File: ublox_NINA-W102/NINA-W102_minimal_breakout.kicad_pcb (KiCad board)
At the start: 2 copper layers, 47 x 20.7 mm, 17 parts, among them J1 Conn_01x15, J2 Conn_01x15, J3 6_PIN_SERIAL_TARGETLOCK, SW1 BOOT, SW2 RESET, U1 NINA-W102

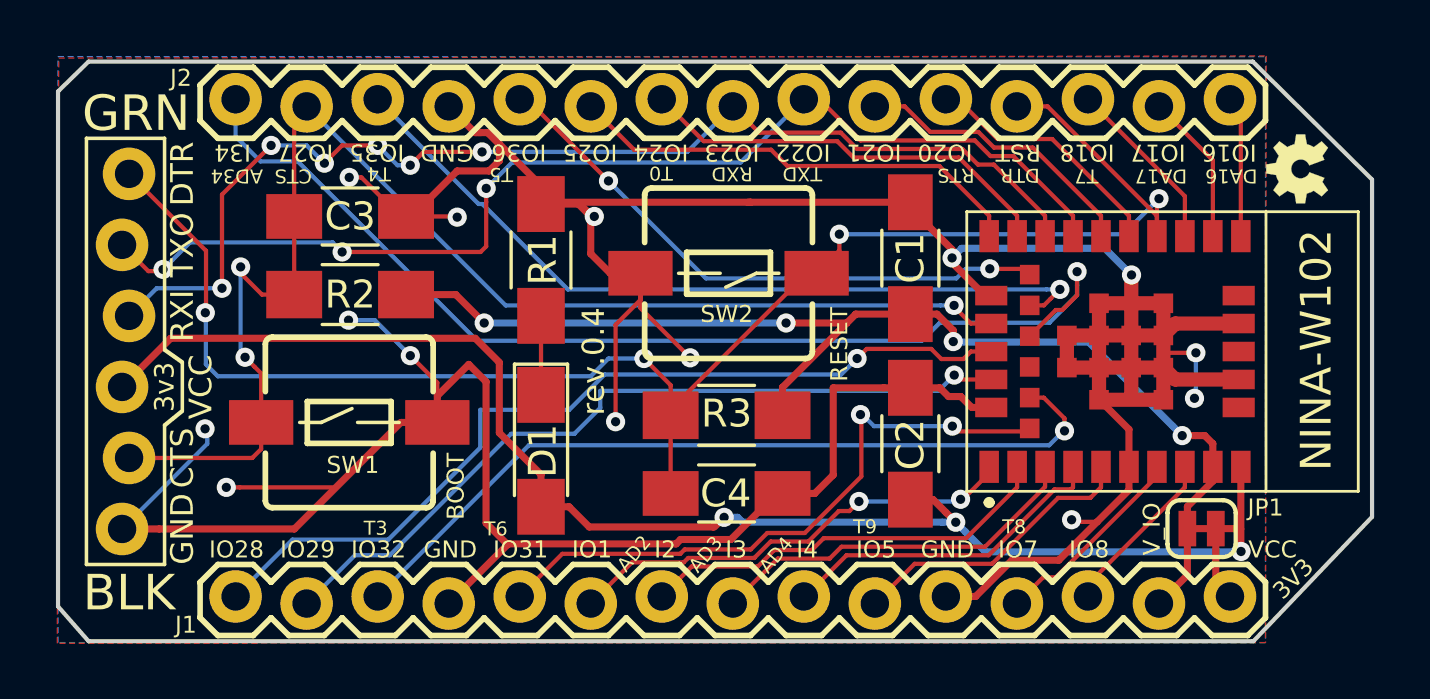
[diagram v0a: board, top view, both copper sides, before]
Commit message: Added some ground vias
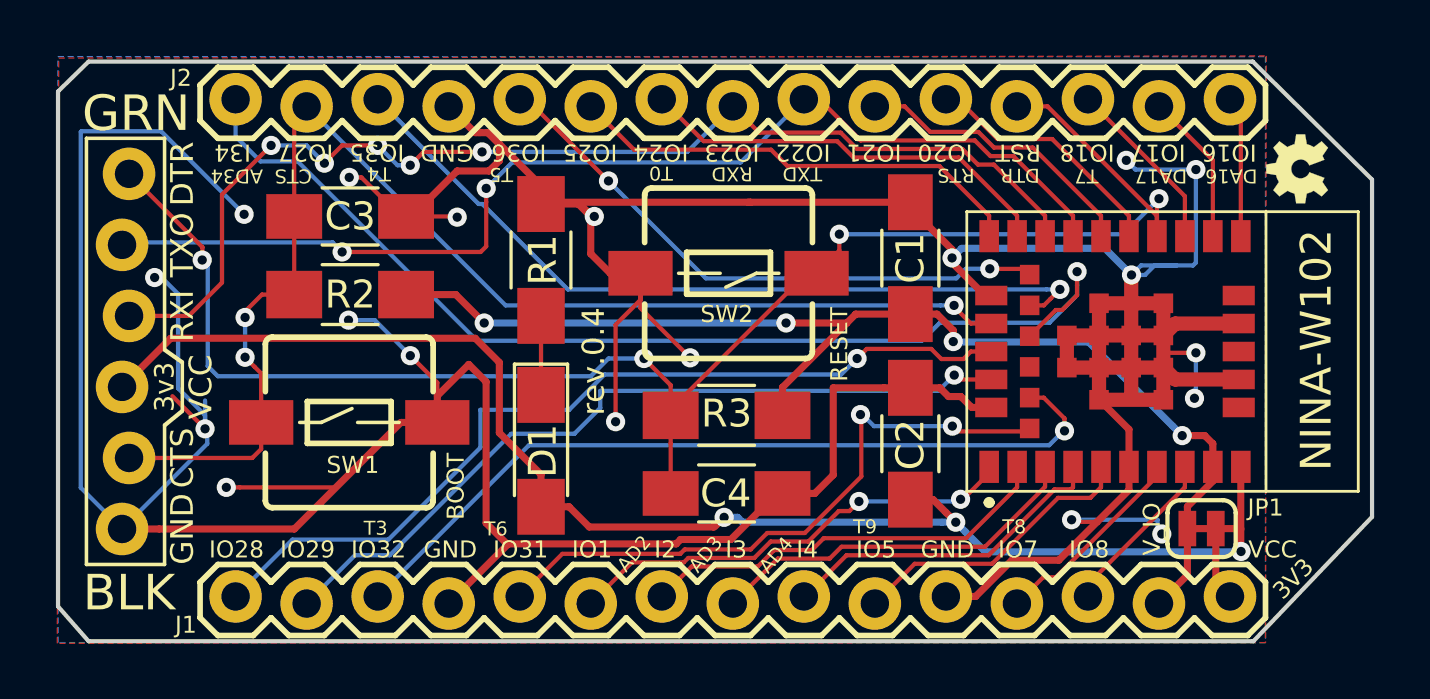
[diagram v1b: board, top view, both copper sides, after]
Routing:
- net GND: track 167.0 -> 211.7 mm, vias 14 -> 19
- net CTS: track 48.8 -> 46.7 mm
- net TXD: track 40.9 -> 40.1 mm, vias 3 -> 2
- net RXD: track 41.3 -> 41.2 mm, vias 6 -> 5

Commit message: Additions and changes to the labeling
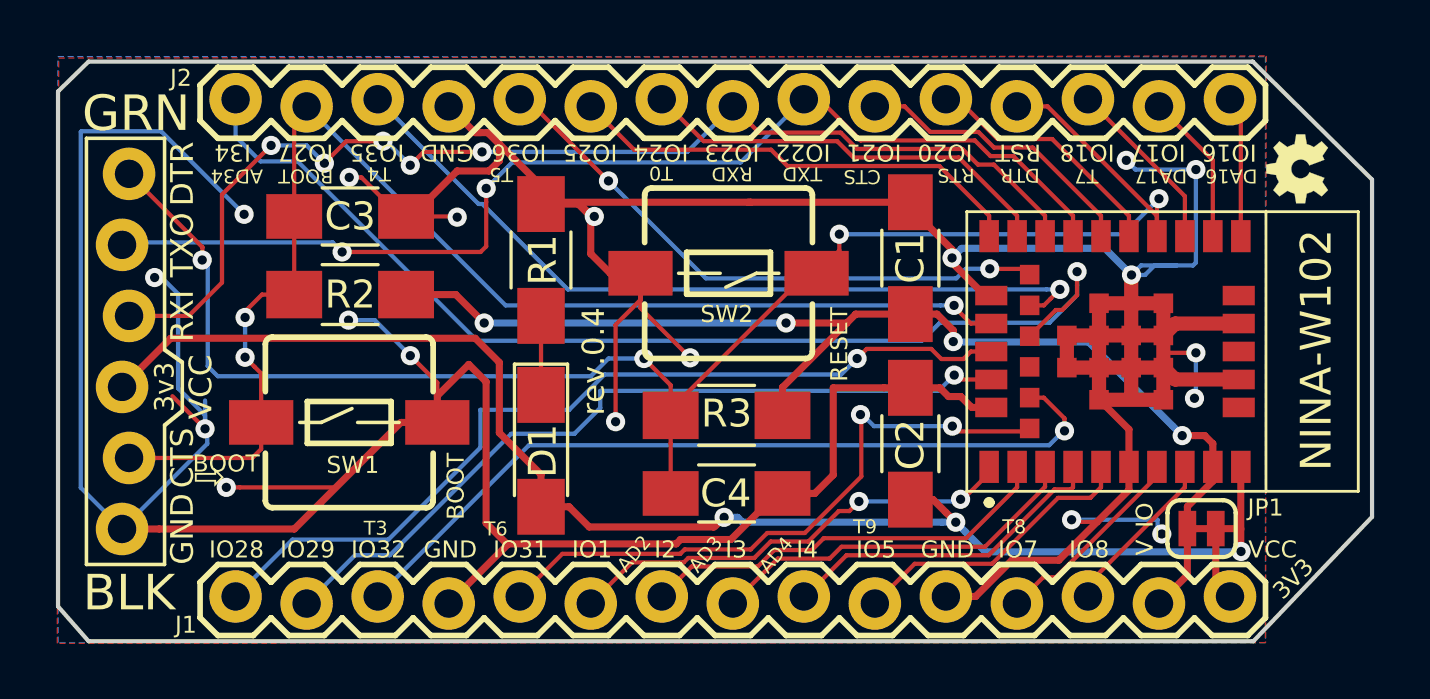
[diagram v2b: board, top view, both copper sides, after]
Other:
- board text added: "BOOT"
- board text added: "⇨"
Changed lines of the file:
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@@
     (area 104.064999 95.987799 151.205001 116.864201)
     (thickness 1.6)
-    (drawings 63)
-    (tracks 486)
+    (drawings 66)
+    (tracks 487)
     (zones 0)
     (modules 17)
@@
       (xy 0.88646 0.23114)) (layer F.SilkS) (width 0.01))
   )
+  (gr_text ⇨ (at 110.1344 110.8964) (layer F.SilkS)
+    (effects (font (size 1 1) (thickness 0.05)) (justify right))
+  )
+  (gr_text BOOT (at 111.3536 110.4392) (layer F.SilkS)
+    (effects (font (size 0.6096 0.6096) (thickness 0.05)) (justify right))
+  )
+  (gr_text CTS (at 132.2324 100.1776 180) (layer F.SilkS)
+    (effects (font (size 0.5 0.5) (thickness 0.12)) (justify right))
+  )
   (dimension 2.5654 (width 0.3) (layer Eco2.User)
     (gr_text "2.565 mm" (at 173 93.6625 90) (layer Eco2.User)
@@
     (effects (font (size 0.5 0.5) (thickness 0.12)) (justify right))
   )
-  (gr_text CTS (at 111.887 100.1522 180) (layer F.SilkS)
+  (gr_text BOOT (at 112.014 100.1522 180) (layer F.SilkS)
     (effects (font (size 0.5 0.5) (thickness 0.12)) (justify right))
   )
@@
     (effects (font (size 0.6096 0.6096) (thickness 0.127)))
   )
-  (gr_text V_IO (at 143.256 112.776 90) (layer F.SilkS)
+  (gr_text V_IO (at 143.002 112.776 90) (layer F.SilkS)
     (effects (font (size 0.6096 0.6096) (thickness 0.127)))
   )
@@
   (segment (start 138.437 101.5776) (end 136.351234 99.491834) (width 0.1524) (layer F.Cu) (net 21))
   (segment (start 136.351234 99.491834) (end 132.587466 99.491834) (width 0.1524) (layer F.Cu) (net 21))
+  (segment (start 114.450597 98.909403) (end 115.276793 98.909403) (width 0.1524) (layer F.Cu) (net 22))
+  (segment (start 115.276793 98.909403) (end 115.761726 98.909403) (width 0.1524) (layer F.Cu) (net 22))
+  (segment (start 113.665 99.695) (end 114.450597 98.909403) (width 0.1524) (layer F.Cu) (net 22))
+  (segment (start 115.876666 98.909403) (end 115.761726 98.909403) (width 0.1524) (layer B.Cu) (net 22))
+  (segment (start 116.736413 99.76915) (end 115.876666 98.909403) (width 0.1524) (layer B.Cu) (net 22))
+  (via (at 115.761726 98.909403) (size 0.6858) (drill 0.3302) (layers F.Cu B.Cu) (net 22))
   (segment (start 111.76 99.06) (end 110.003787 100.816213) (width 0.1524) (layer F.Cu) (net 22))
   (segment (start 110.003787 100.816213) (end 110.003787 103.965813) (width 0.1524) (layer F.Cu) (net 22))
@@
   (segment (start 128.27 97.663) (end 126.640805 99.292195) (width 0.1524) (layer B.Cu) (net 22))
   (segment (start 126.640805 99.292195) (end 119.788061 99.292195) (width 0.1524) (layer B.Cu) (net 22))
-  (segment (start 116.27915 99.76915) (end 116.736413 99.76915) (width 0.1524) (layer B.Cu) (net 22))
-  (segment (start 115.57 99.06) (end 116.27915 99.76915) (width 0.1524) (layer B.Cu) (net 22))
   (via (at 116.736413 99.76915) (size 0.6858) (drill 0.3302) (layers F.Cu B.Cu) (net 22))
   (via (at 111.76 99.06) (size 0.6858) (drill 0.3302) (layers F.Cu B.Cu) (net 22))
   (segment (start 113.665 99.695) (end 113.03 99.06) (width 0.1524) (layer B.Cu) (net 22))
   (segment (start 113.03 99.06) (end 111.76 99.06) (width 0.1524) (layer B.Cu) (net 22))
-  (segment (start 115.57 99.06) (end 114.3 99.06) (width 0.1524) (layer F.Cu) (net 22))
   (via (at 113.665 99.695) (size 0.6858) (drill 0.3302) (layers F.Cu B.Cu) (net 22))
-  (segment (start 114.3 99.06) (end 113.665 99.695) (width 0.1524) (layer F.Cu) (net 22))
-  (via (at 115.57 99.06) (size 0.6858) (drill 0.3302) (layers F.Cu B.Cu) (net 22))
   (segment (start 114.3 102.87) (end 113.957101 102.527101) (width 0.1524) (layer B.Cu) (net 23))
   (segment (start 113.957101 102.527101) (end 106.496729 102.527101) (width 0.1524) (layer B.Cu) (net 23))

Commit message: Added some MakeZurich artwork
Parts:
- added MakeZurich-15x11-silk: G***, lib:MakeZurich-15x11-silk, B.Cu at (142.1, 107.7)
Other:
- board text added: "Rev.0.4"
- board text added: "ublox NINA-W102 minimal breakout"
- board text added: "www.rac.su"

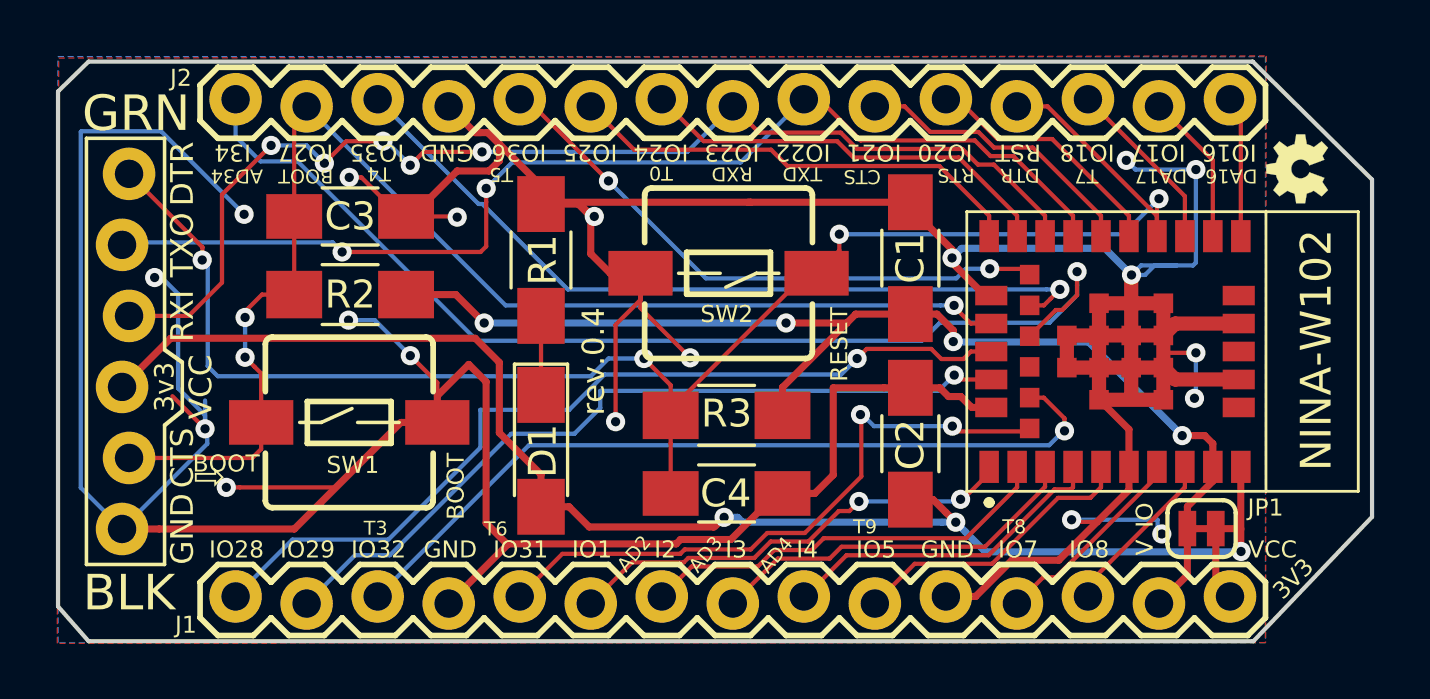
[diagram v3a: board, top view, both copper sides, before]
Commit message: DuckTape approved stamp and track angle corrections and some more ground vias
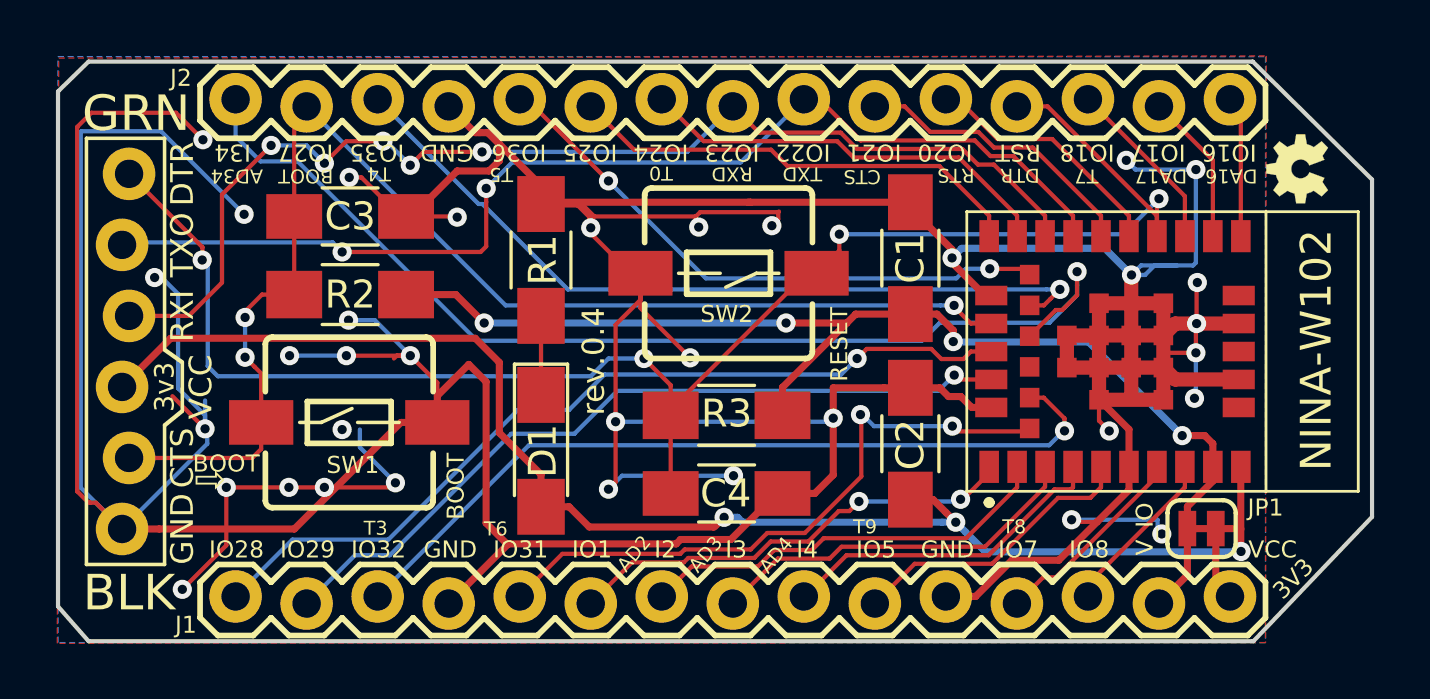
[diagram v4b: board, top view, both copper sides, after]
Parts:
- added G***: LOGO, lib:DuckTapeApproved-13x13, B.Cu at (127.3, 107.7)
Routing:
- net GND: track 211.7 -> 272.4 mm, vias 19 -> 34
- net Net-(J1-Pad1): track 31.7 -> 30.9 mm
- net (no net): vias 0 -> 1

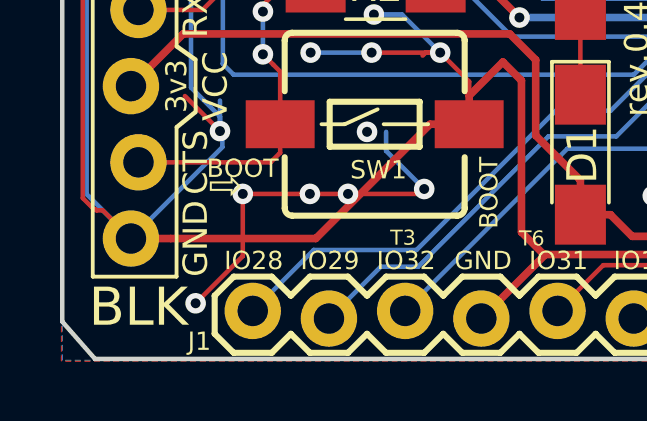
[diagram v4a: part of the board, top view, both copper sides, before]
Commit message: Added footprints to local library and reassigned in schematic
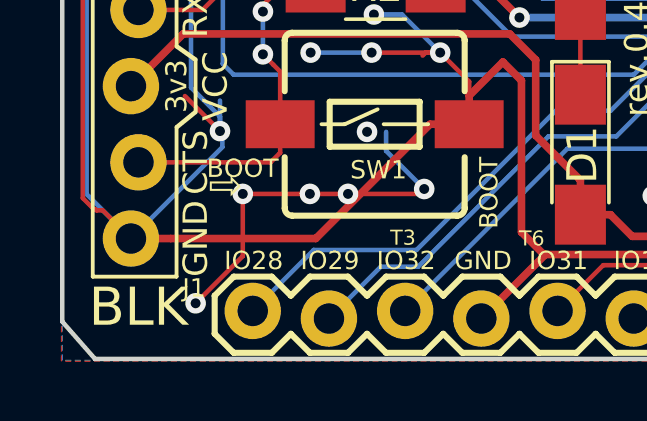
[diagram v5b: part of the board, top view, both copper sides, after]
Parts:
- J1, J2: footprint Connectors-SparkFun:1X15_LOCK -> lib:1X15_LOCK
- JP1: footprint Jumpers:SMT-JUMPER_2_NC_TRACE_SILK -> lib:SMT-JUMPER_2_NC_TRACE_SILK

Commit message: Change duck tape silkscreen for licensed one ;)
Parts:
- G***: footprint lib:DuckTapeApproved-13x13 -> lib:DuckTapeApproved-MIT
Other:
- net class Default: trace_width 0.1524 -> 0.25
- board text added: "Rev.0.5"
- board text removed: "Rev.0.4"
